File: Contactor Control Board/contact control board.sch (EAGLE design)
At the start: 32 parts, among them Q4 MOSFET-NCHANNELFQP30N06L, U1 74ACT14SC

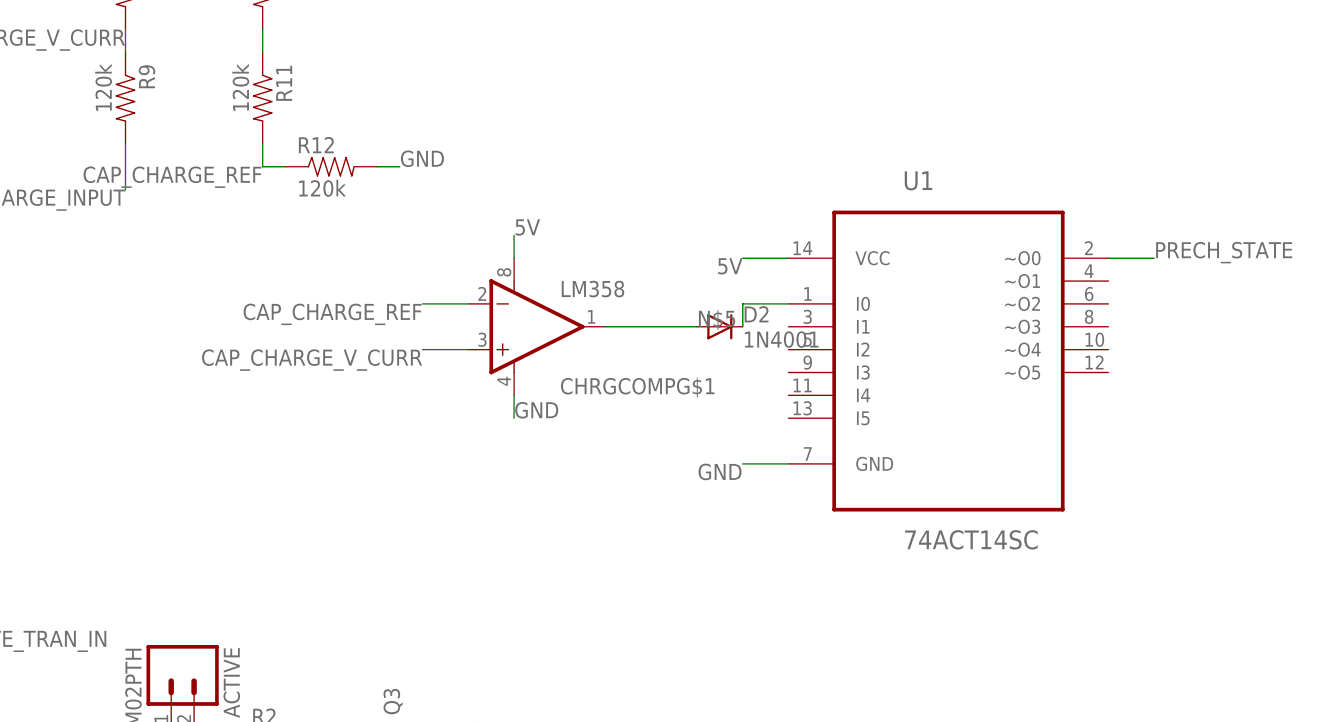
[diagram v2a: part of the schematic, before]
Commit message: Replaced op-amp with voltage comparitor. Need to redo the voltage dividers for a 0-18V range or similar instead of 0-5V
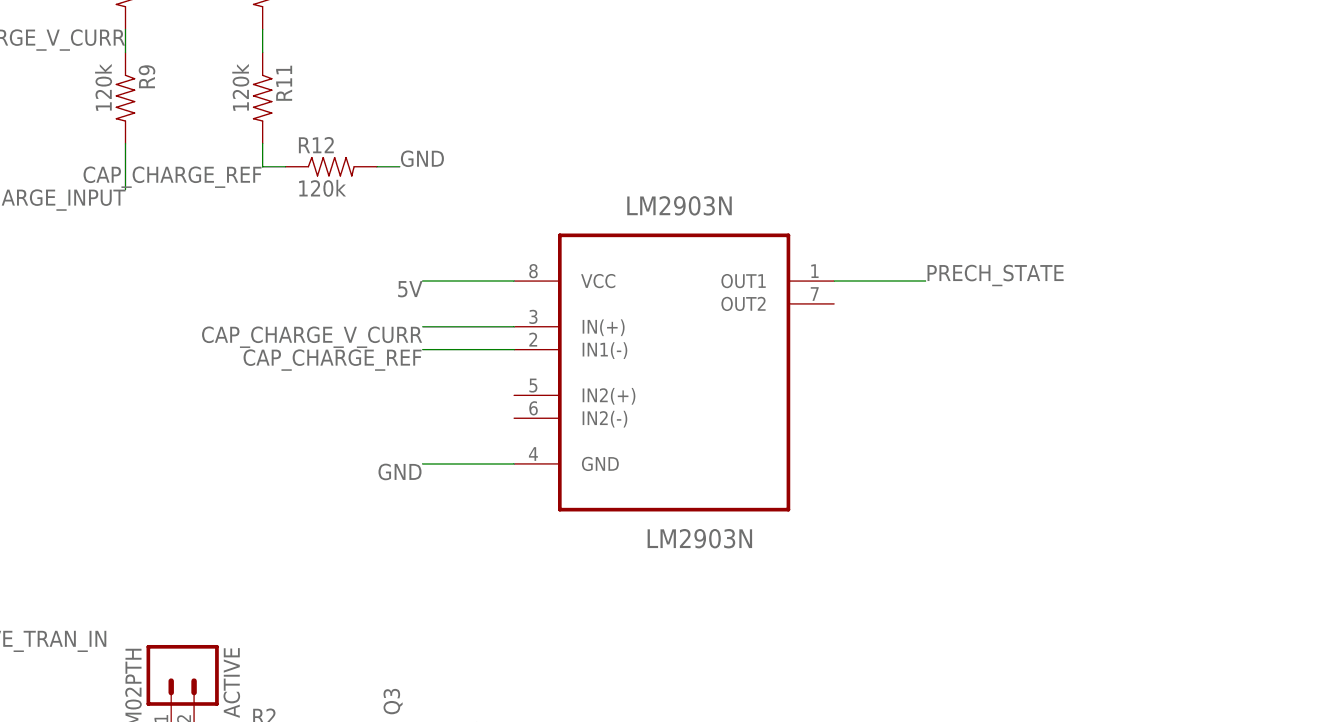
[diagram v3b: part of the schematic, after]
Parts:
- removed CHRGCOMP: LM358, SparkFun-AnalogIC:LM358
- removed D2: 1N4001, SparkFun-DiscreteSemi:DIODEPTH
- removed U1: 74ACT14SC, Fairchild_By_element14_Batch_1:74ACT14SC
- added LM2903N: LM2903N, Fairchild_By_element14_Batch_1:LM2903N
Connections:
- removed net N$5: CHRGCOMPG$1.OUT, D2.A
- removed net N$6: U1.I0
- net 5V: now also LM2903N.VCC; no longer CHRGCOMPG$1.V+, U1.VCC
- net CAP_CHARGE_REF: no longer CHRGCOMPG$1.-IN
- net CAP_CHARGE_V_CURR: no longer CHRGCOMPG$1.+IN
- net GND: now also LM2903N.GND; no longer CHRGCOMPG$1.V-, U1.GND
- net PRECH_STATE: now also LM2903N.OUT1; no longer U1.~O0
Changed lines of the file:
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@@
 <part name="RESISTOR" library="SparkFun-Connectors" deviceset="M02" device="2.54MM_SCREWTERM"/>
 <part name="JP1" library="SparkFun-Connectors" deviceset="M09" device=""/>
-<part name="CHRGCOMP" library="SparkFun-AnalogIC" deviceset="LM358" device=""/>
-<part name="D2" library="SparkFun-DiscreteSemi" deviceset="DIODE" device="PTH" value="1N4001"/>
 <part name="R8" library="SparkFun-Resistors" deviceset="RESISTOR" device="PTH-1/4W" value="3M"/>
 <part name="R9" library="SparkFun-Resistors" deviceset="RESISTOR" device="PTH-1/4W" value="120k"/>
@@
 <part name="R11" library="SparkFun-Resistors" deviceset="RESISTOR" device="PTH-1/4W" value="120k"/>
 <part name="R12" library="SparkFun-Resistors" deviceset="RESISTOR" device="PTH-1/4W" value="120k"/>
-<part name="U1" library="Fairchild_By_element14_Batch_1" deviceset="74ACT14SC" device=""/>
+<part name="LM2903N" library="Fairchild_By_element14_Batch_1" deviceset="LM2903N" device=""/>
 </parts>
 <sheets>
@@
 <instance part="RESISTOR" gate="G$1" x="53.34" y="114.3" rot="R180"/>
 <instance part="JP1" gate="G$1" x="116.84" y="50.8"/>
-<instance part="CHRGCOMP" gate="G$1" x="114.3" y="121.92"/>
-<instance part="D2" gate="G$1" x="137.16" y="121.92"/>
 <instance part="R8" gate="G$1" x="71.12" y="160.02" rot="R270"/>
 <instance part="R9" gate="G$1" x="71.12" y="147.32" rot="R270"/>
@@
 <instance part="R11" gate="G$1" x="86.36" y="147.32" rot="R270"/>
 <instance part="R12" gate="G$1" x="93.98" y="139.7"/>
-<instance part="U1" gate="A" x="162.56" y="121.92"/>
+<instance part="LM2903N" gate="A" x="132.08" y="119.38"/>
 </instances>
 <busses>
@@
 </segment>
 <segment>
-<pinref part="CHRGCOMP" gate="G$1" pin="V+"/>
-<wire x1="114.3" y1="129.54" x2="114.3" y2="132.08" width="0.2032" layer="91"/>
-<label x="114.3" y="132.08" size="1.778" layer="95"/>
-</segment>
-<segment>
-<pinref part="U1" gate="A" pin="VCC"/>
-<wire x1="144.78" y1="129.54" x2="139.7" y2="129.54" width="0.2032" layer="91"/>
-<label x="139.7" y="129.54" size="1.778" layer="95" rot="R180"/>
+<pinref part="LM2903N" gate="A" pin="VCC"/>
+<wire x1="114.3" y1="127" x2="104.14" y2="127" width="0.2032" layer="91"/>
+<label x="104.14" y="127" size="1.778" layer="95" rot="R180"/>
 </segment>
 </net>
@@
 </segment>
 <segment>
-<pinref part="CHRGCOMP" gate="G$1" pin="V-"/>
-<wire x1="114.3" y1="114.3" x2="114.3" y2="111.76" width="0.2032" layer="91"/>
-<label x="114.3" y="111.76" size="1.778" layer="95"/>
-</segment>
-<segment>
 <pinref part="OUTPUT" gate="G$1" pin="5"/>
 <wire x1="-5.08" y1="50.8" x2="-10.16" y2="50.8" width="0.2032" layer="91"/>
@@
 </segment>
 <segment>
-<pinref part="U1" gate="A" pin="GND"/>
-<wire x1="144.78" y1="106.68" x2="139.7" y2="106.68" width="0.2032" layer="91"/>
-<label x="139.7" y="106.68" size="1.778" layer="95" rot="R180"/>
+<pinref part="LM2903N" gate="A" pin="GND"/>
+<wire x1="114.3" y1="106.68" x2="104.14" y2="106.68" width="0.2032" layer="91"/>
+<label x="104.14" y="106.68" size="1.778" layer="95" rot="R180"/>
 </segment>
 </net>
@@
 </segment>
 <segment>
-<pinref part="U1" gate="A" pin="~O0"/>
-<wire x1="180.34" y1="129.54" x2="185.42" y2="129.54" width="0.2032" layer="91"/>
-<label x="185.42" y="129.54" size="1.778" layer="95"/>
+<pinref part="LM2903N" gate="A" pin="OUT1"/>
+<wire x1="149.86" y1="127" x2="160.02" y2="127" width="0.2032" layer="91"/>
+<label x="160.02" y="127" size="1.778" layer="95"/>
 </segment>
 </net>
@@
 </segment>
 </net>
-<net name="N$5" class="0">
-<segment>
-<pinref part="CHRGCOMP" gate="G$1" pin="OUT"/>
-<wire x1="124.46" y1="121.92" x2="134.62" y2="121.92" width="0.2032" layer="91"/>
-<label x="134.62" y="121.92" size="1.778" layer="95"/>
-<pinref part="D2" gate="G$1" pin="A"/>
-</segment>
-</net>
 <net name="CAP_CHARGE_REF" class="0">
 <segment>
-<pinref part="CHRGCOMP" gate="G$1" pin="-IN"/>
-<wire x1="109.22" y1="124.46" x2="104.14" y2="124.46" width="0.2032" layer="91"/>
-<label x="104.14" y="124.46" size="1.778" layer="95" rot="R180"/>
+<wire x1="114.3" y1="119.38" x2="104.14" y2="119.38" width="0.2032" layer="91"/>
+<label x="104.14" y="119.38" size="1.778" layer="95" rot="R180"/>
 </segment>
 <segment>
@@
 </segment>
 <segment>
-<pinref part="CHRGCOMP" gate="G$1" pin="+IN"/>
-<wire x1="109.22" y1="119.38" x2="104.14" y2="119.38" width="0.2032" layer="91"/>
-<label x="104.14" y="119.38" size="1.778" layer="95" rot="R180"/>
-</segment>
-</net>
-<net name="N$6" class="0">
-<segment>
-<pinref part="U1" gate="A" pin="I0"/>
-<wire x1="144.78" y1="124.46" x2="139.7" y2="124.46" width="0.2032" layer="91"/>
-<wire x1="139.7" y1="121.92" x2="139.7" y2="124.46" width="0.2032" layer="91"/>
-</segment>
-</net>
+<wire x1="114.3" y1="121.92" x2="104.14" y2="121.92" width="0.2032" layer="91"/>
+<label x="104.14" y="121.92" size="1.778" layer="95" rot="R180"/>
+</segment>
+</net>

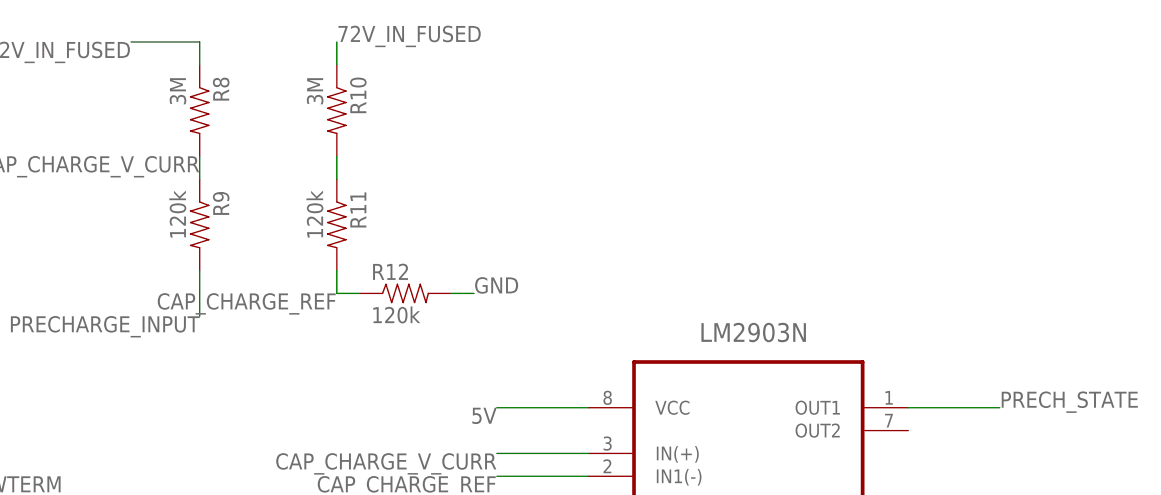
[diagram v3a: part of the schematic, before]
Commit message: Updating voltage dividers to common resistor values
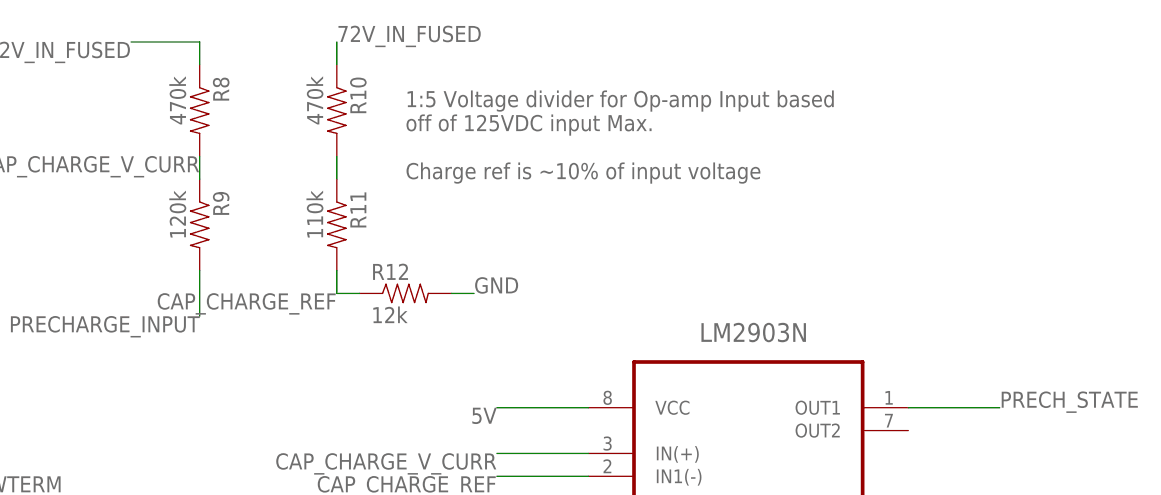
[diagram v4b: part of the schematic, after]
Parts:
- R10, R8: value 3M -> 470k
- R11: value 120k -> 110k
- R12: value 120k -> 12k
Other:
- note added: "1:5 Voltage divider for Op-amp Input based off of 125VDC input Max. Charge ref is ~10% of input voltage"
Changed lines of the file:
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@@
 <part name="RESISTOR" library="SparkFun-Connectors" deviceset="M02" device="2.54MM_SCREWTERM"/>
 <part name="JP1" library="SparkFun-Connectors" deviceset="M09" device=""/>
-<part name="R8" library="SparkFun-Resistors" deviceset="RESISTOR" device="PTH-1/4W" value="3M"/>
+<part name="R8" library="SparkFun-Resistors" deviceset="RESISTOR" device="PTH-1/4W" value="470k"/>
 <part name="R9" library="SparkFun-Resistors" deviceset="RESISTOR" device="PTH-1/4W" value="120k"/>
-<part name="R10" library="SparkFun-Resistors" deviceset="RESISTOR" device="PTH-1/4W" value="3M"/>
-<part name="R11" library="SparkFun-Resistors" deviceset="RESISTOR" device="PTH-1/4W" value="120k"/>
-<part name="R12" library="SparkFun-Resistors" deviceset="RESISTOR" device="PTH-1/4W" value="120k"/>
+<part name="R10" library="SparkFun-Resistors" deviceset="RESISTOR" device="PTH-1/4W" value="470k"/>
+<part name="R11" library="SparkFun-Resistors" deviceset="RESISTOR" device="PTH-1/4W" value="110k"/>
+<part name="R12" library="SparkFun-Resistors" deviceset="RESISTOR" device="PTH-1/4W" value="12k"/>
 <part name="LM2903N" library="Fairchild_By_element14_Batch_1" deviceset="LM2903N" device=""/>
 </parts>
@@
 <sheet>
 <plain>
+<text x="93.98" y="152.4" size="1.778" layer="95">1:5 Voltage divider for Op-amp Input based
+off of 125VDC input Max.
+Charge ref is ~10% of input voltage</text>
 </plain>
 <instances>
@@
 </schematic>
 </drawing>
+<compatibility>
+<note version="6.3" minversion="6.2.2" severity="warning">
+Since Version 6.2.2 text objects can contain more than one line,
+which will not be processed correctly with this version.
+</note>
+</compatibility>
 </eagle>

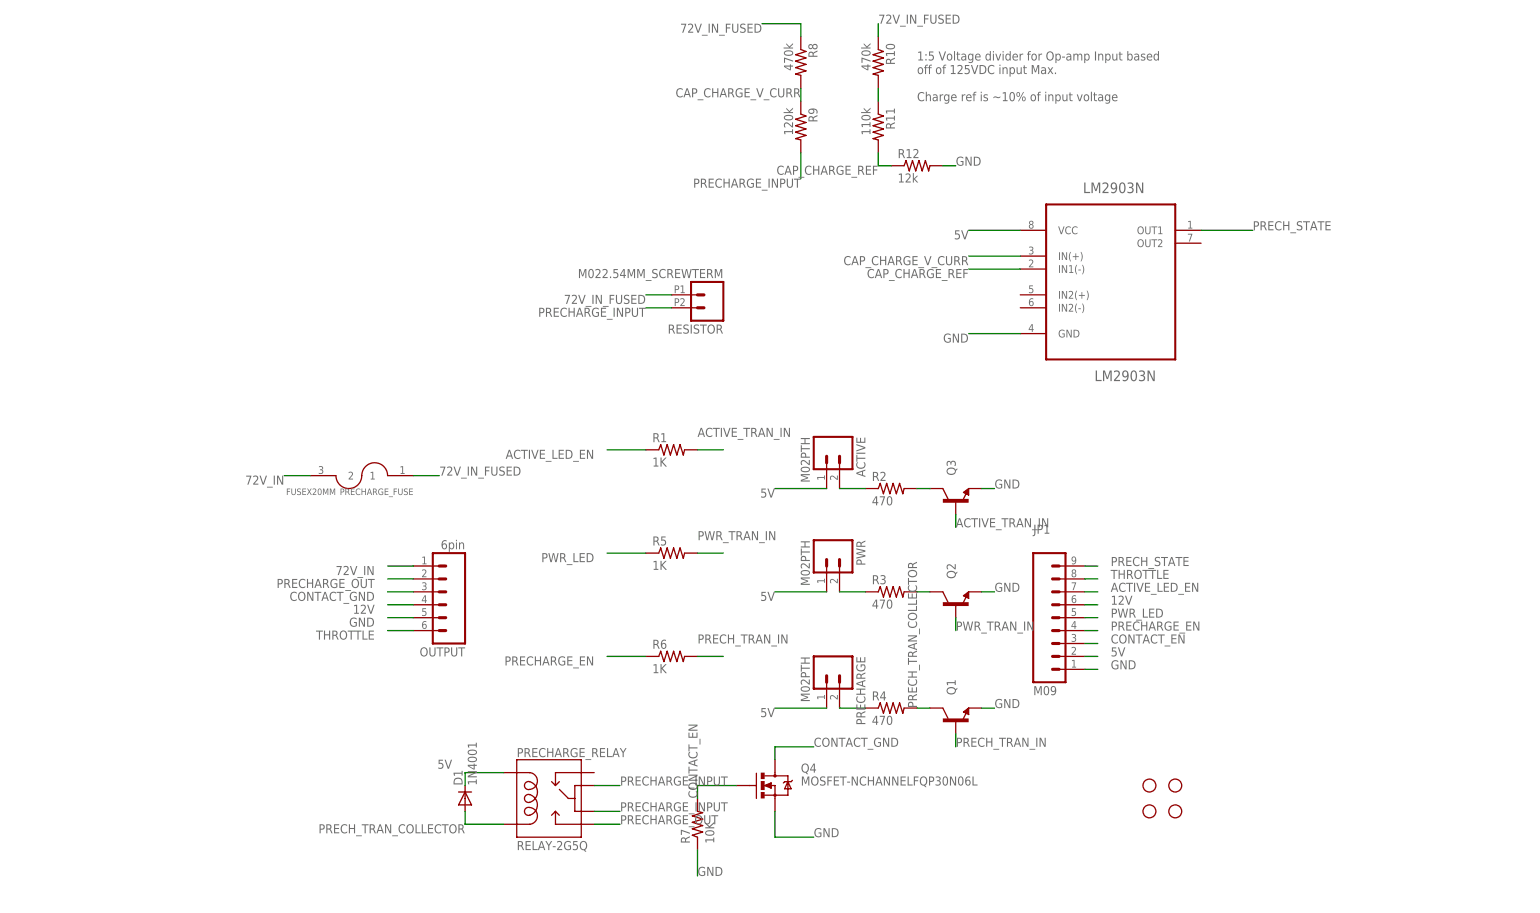
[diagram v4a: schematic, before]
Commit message: Final draft design for CCB (thru-hole) before proto-boarding.
Replaced SPST relay with DPDT relay so that its NC connections will
drain the capacitors and its NO connections will charge them. This way
we can wait a shorter period of time after powering down the machine
before servicing!
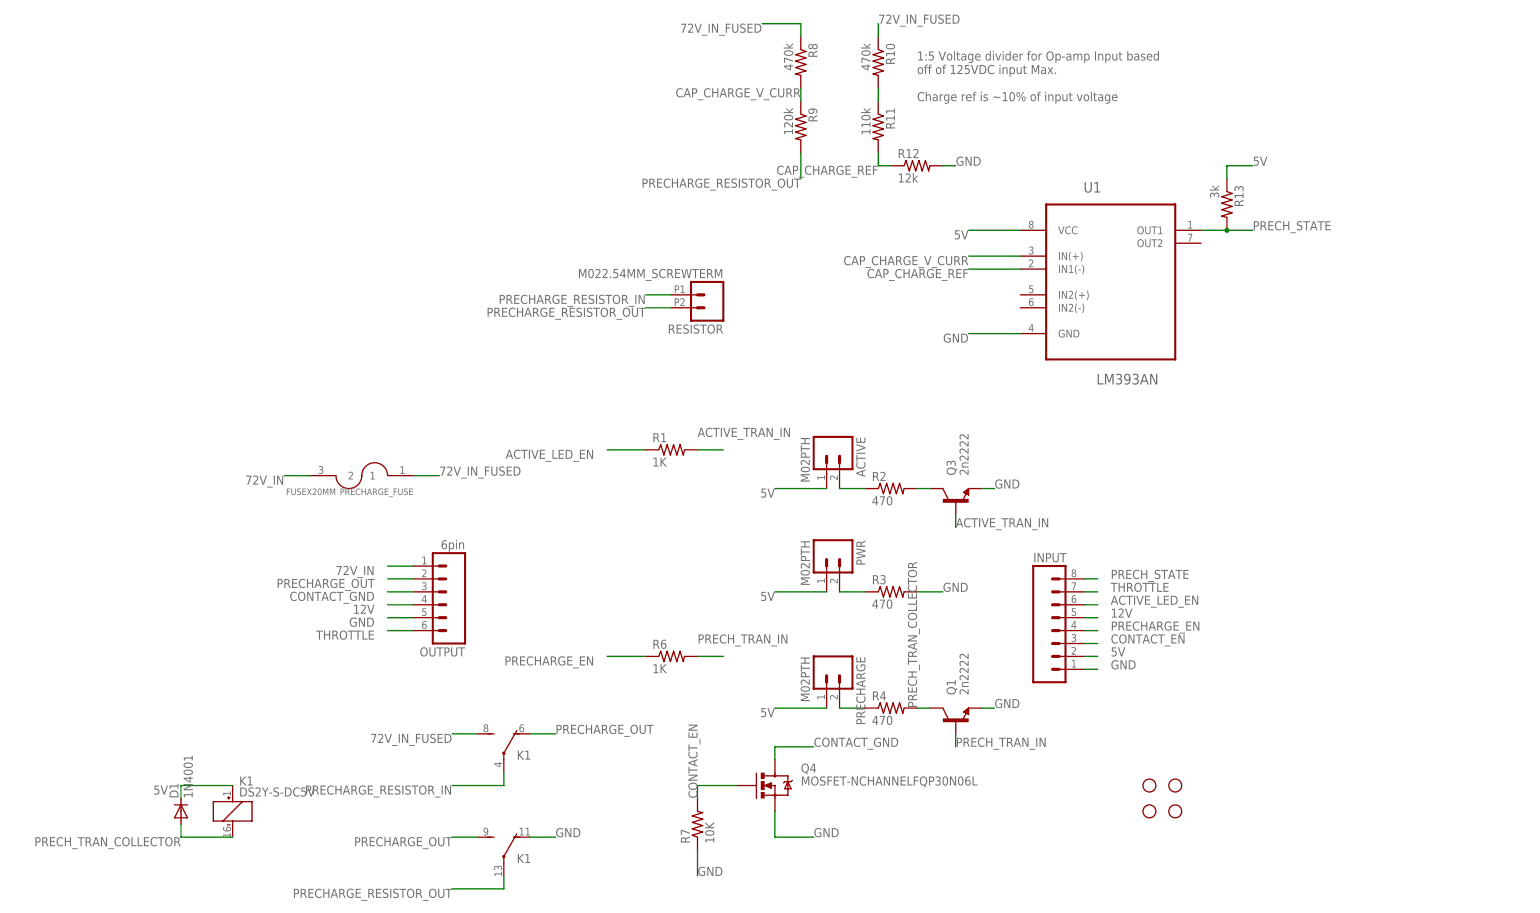
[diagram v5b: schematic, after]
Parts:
- removed JP1: M09, SparkFun-Connectors:M09
- removed LM2903N: LM2903N, Fairchild_By_element14_Batch_1:LM2903N
- removed PRECHARGE_RELAY: RELAY-2G5Q, SparkFun-Electromechanical:RELAY-2G5Q
- removed Q2: (no value), SparkFun-DiscreteSemi:TRANSISTOR_NPNTO92
- removed R5: 1K, SparkFun-Resistors:RESISTORPTH-1/4W
- added INPUT: (no value), SparkFun-Connectors:M081X08
- added K1: DS2Y-S-DC5V, relay:DS2Y-S-DC5V
- added R13: 3k, SparkFun-Resistors:RESISTORPTH-1/4W
- added U1: LM393AN, Fairchild_By_element14_Batch_1:LM393AN
- Q1, Q3: value (none) -> 2n2222
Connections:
- removed net N$2: Q2.C, R3.2
- removed net PRECHARGE_INPUT: PRECHARGE_RELAY.5, PRECHARGE_RELAY.6, R9.2, RESISTOR.2
- removed net PWR_LED: JP1.5, R5.1
- removed net PWR_TRAN_IN: Q2.B, R5.2
- new net PRECHARGE_RESISTOR_IN: K12.P, RESISTOR.1
- new net PRECHARGE_RESISTOR_OUT: K13.P, R9.2, RESISTOR.2
- net 12V: now also INPUT.5; no longer JP1.6
- net 5V: now also INPUT.2, K11.+, R13.1, U1.VCC; no longer JP1.2, LM2903N.VCC, PRECHARGE_RELAY.2
- net 72V_IN_FUSED: now also K12.S; no longer RESISTOR.1
- net ACTIVE_LED_EN: now also INPUT.6; no longer JP1.7
- net CAP_CHARGE_REF: now also U1.IN1(-)
- net CAP_CHARGE_V_CURR: now also U1.IN(+)
- net CONTACT_EN: now also INPUT.3; no longer JP1.3
- net GND: now also INPUT.1, K13.O, R3.2, U1.GND; no longer JP1.1, LM2903N.GND, Q2.E
- net PRECHARGE_EN: now also INPUT.4; no longer JP1.4
- net PRECHARGE_OUT: now also K12.O, K13.S; no longer PRECHARGE_RELAY.10
- net PRECH_STATE: now also INPUT.8, R13.2, U1.OUT1; no longer JP1.9, LM2903N.OUT1
- net PRECH_TRAN_COLLECTOR: now also K11.-; no longer PRECHARGE_RELAY.9
- net THROTTLE: now also INPUT.7; no longer JP1.8
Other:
- moved on the sheet: D1
